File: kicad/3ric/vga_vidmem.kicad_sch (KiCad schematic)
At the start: 13 parts

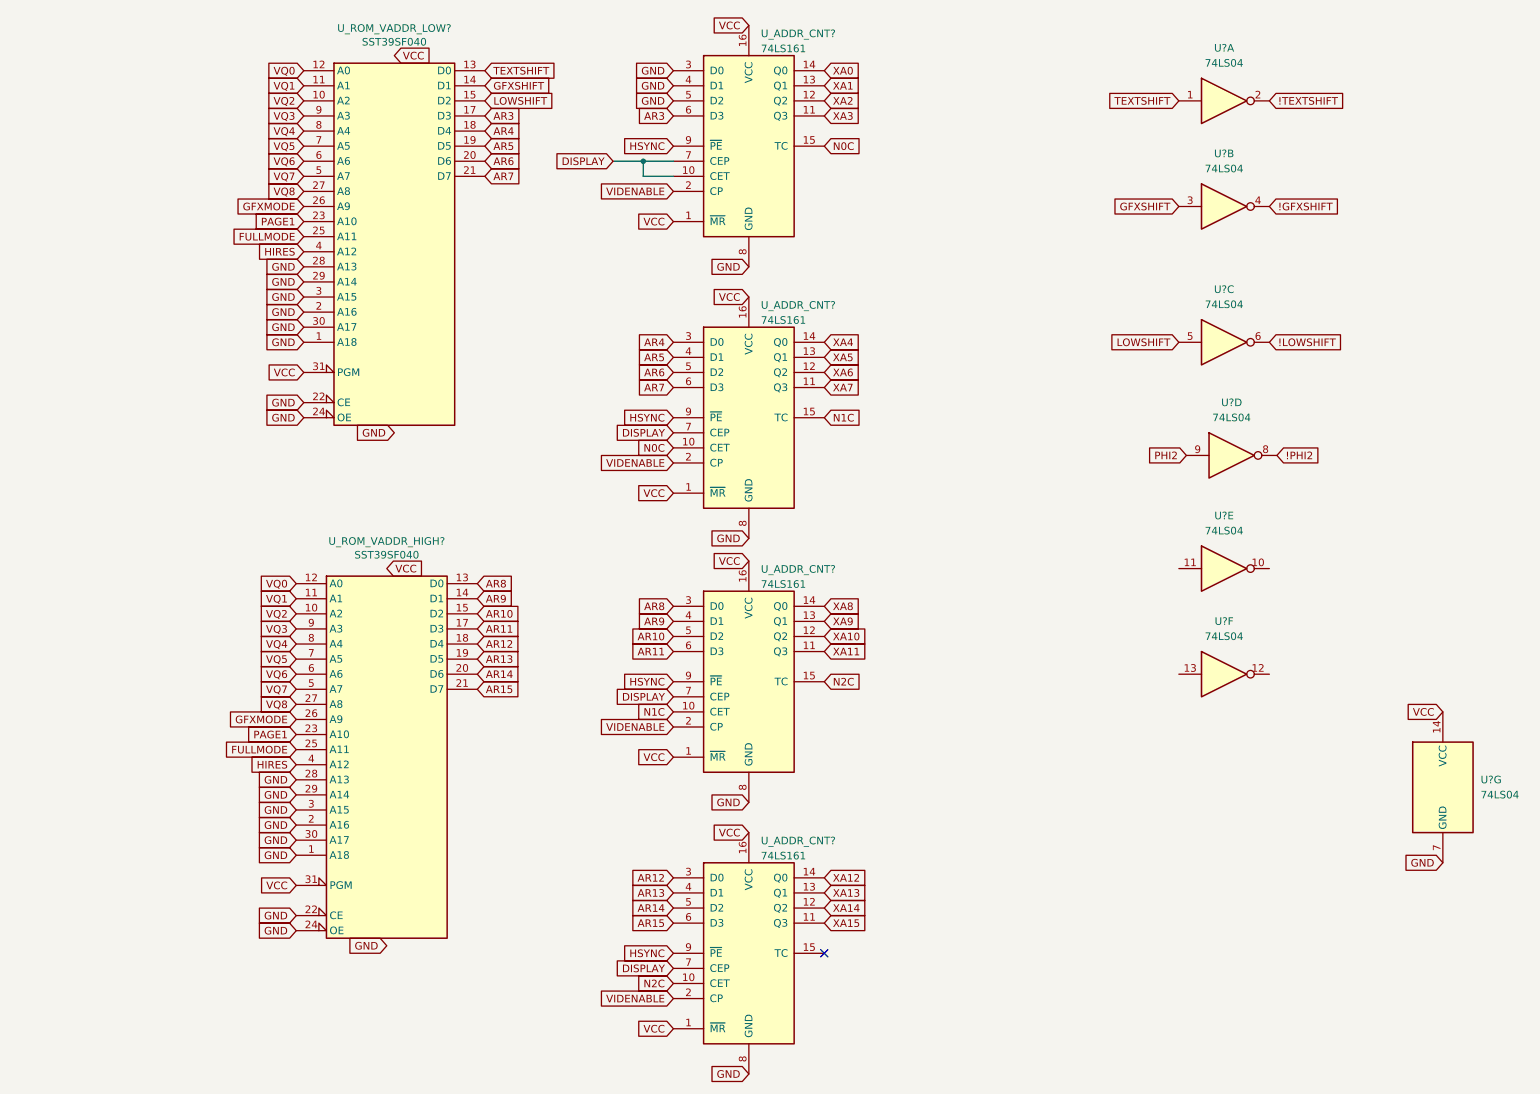
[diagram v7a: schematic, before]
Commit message: update schematic based on breadboard
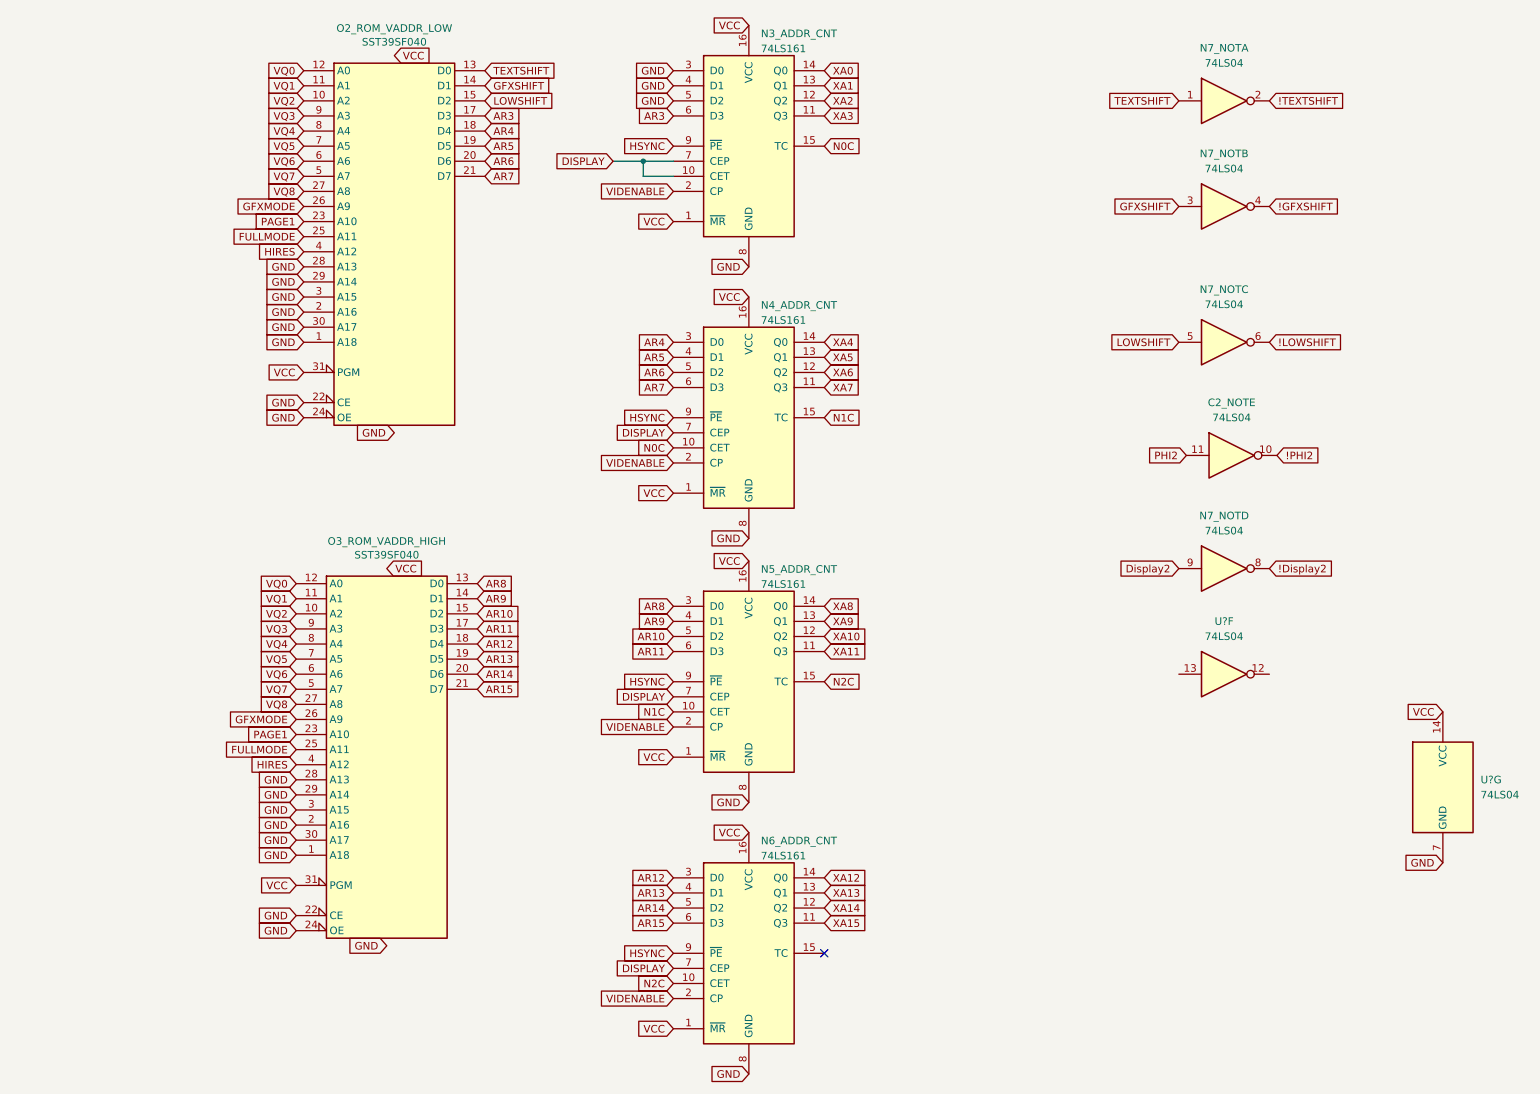
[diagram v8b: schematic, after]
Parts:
- gave numbers to parts that had none: 8
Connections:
- net !PHI2: now also C2_NOT.10; no longer C2_NOT.8
- net PHI2: now also C2_NOT.11; no longer C2_NOT.9
- new net !Display2: N7_NOT.8
- new net Display2: N7_NOT.9
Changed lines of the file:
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@@
 		)
 	)
+	(global_label "!Display2"
+		(shape input)
+		(at 233.68 109.22 0)
+		(fields_autoplaced yes)
+		(effects
+			(font
+				(size 1.27 1.27)
+			)
+			(justify left)
+		)
+		(property "Intersheetrefs" "${INTERSHEET_REFS}"
+			(at 245.3132 109.22 0)
+			(effects
+				(font
+					(size 1.27 1.27)
+				)
+				(justify left)
+				(hide yes)
+			)
+		)
+	)
 	(global_label "VQ2"
 		(shape input)
@@
 		)
 	)
+	(global_label "Display2"
+		(shape input)
+		(at 218.44 109.22 180)
+		(fields_autoplaced yes)
+		(effects
+			(font
+				(size 1.27 1.27)
+			)
+			(justify right)
+		)
+		(property "Intersheetrefs" "${INTERSHEET_REFS}"
+			(at 207.4116 109.22 0)
+			(effects
+				(font
+					(size 1.27 1.27)
+				)
+				(justify right)
+				(hide yes)
+			)
+		)
+	)
 	(global_label "VQ2"
 		(shape input)
@@
 		(on_board yes)
 		(dnp no)
-		(property "Reference" "U_ROM_VADDR_LOW?"
+		(property "Reference" "O2_ROM_VADDR_LOW"
 			(at 86.36 18.2626 0)
 			(effects
@@
 			(project "3ric"
 				(path "/e63e39d7-6ac0-4ffd-8aa3-1841a4541b55/3a5ec449-df9a-4784-a739-e66dc5cc26a2"
-					(reference "U_ROM_VADDR_LOW?")
+					(reference "O2_ROM_VADDR_LOW")
 					(unit 1)
 				)
@@
 		(dnp no)
 		(fields_autoplaced yes)
-		(property "Reference" "U?"
+		(property "Reference" "N7_NOT"
 			(at 226.06 39.37 0)
 			(effects
@@
 			(project "3ric"
 				(path "/e63e39d7-6ac0-4ffd-8aa3-1841a4541b55/3a5ec449-df9a-4784-a739-e66dc5cc26a2"
-					(reference "U?")
+					(reference "N7_NOT")
 					(unit 2)
 				)
@@
 		(dnp no)
 		(fields_autoplaced yes)
-		(property "Reference" "U?"
+		(property "Reference" "N7_NOT"
 			(at 226.06 62.23 0)
 			(effects
@@
 			(project "3ric"
 				(path "/e63e39d7-6ac0-4ffd-8aa3-1841a4541b55/3a5ec449-df9a-4784-a739-e66dc5cc26a2"
-					(reference "U?")
+					(reference "N7_NOT")
 					(unit 3)
 				)
@@
 		(on_board yes)
 		(dnp no)
-		(property "Reference" "U_ROM_VADDR_HIGH?"
+		(property "Reference" "O3_ROM_VADDR_HIGH"
 			(at 85.09 104.6226 0)
 			(effects
@@
 			(project "3ric"
 				(path "/e63e39d7-6ac0-4ffd-8aa3-1841a4541b55/3a5ec449-df9a-4784-a739-e66dc5cc26a2"
-					(reference "U_ROM_VADDR_HIGH?")
+					(reference "O3_ROM_VADDR_HIGH")
 					(unit 1)
 				)
@@
 		(lib_id "74xx:74LS04")
 		(at 226.06 109.22 0)
-		(unit 5)
+		(unit 4)
 		(exclude_from_sim no)
 		(in_bom yes)
@@
 		(dnp no)
 		(fields_autoplaced yes)
-		(property "Reference" "U?"
+		(property "Reference" "N7_NOT"
 			(at 226.06 100.33 0)
 			(effects
@@
 			(project "3ric"
 				(path "/e63e39d7-6ac0-4ffd-8aa3-1841a4541b55/3a5ec449-df9a-4784-a739-e66dc5cc26a2"
-					(reference "U?")
-					(unit 5)
+					(reference "N7_NOT")
+					(unit 4)
 				)
 			)
@@
 		(dnp no)
 		(fields_autoplaced yes)
-		(property "Reference" "U_ADDR_CNT?"
+		(property "Reference" "N6_ADDR_CNT"
 			(at 148.0694 155.0502 0)
 			(effects
@@
 			(project "3ric"
 				(path "/e63e39d7-6ac0-4ffd-8aa3-1841a4541b55/3a5ec449-df9a-4784-a739-e66dc5cc26a2"
-					(reference "U_ADDR_CNT?")
+					(reference "N6_ADDR_CNT")
 					(unit 1)
 				)
@@
 		(dnp no)
 		(fields_autoplaced yes)
-		(property "Reference" "U_ADDR_CNT?"
+		(property "Reference" "N3_ADDR_CNT"
 			(at 148.0694 19.1602 0)
 			(effects
@@
 			(project "3ric"
 				(path "/e63e39d7-6ac0-4ffd-8aa3-1841a4541b55/3a5ec449-df9a-4784-a739-e66dc5cc26a2"
-					(reference "U_ADDR_CNT?")
+					(reference "N3_ADDR_CNT")
 					(unit 1)
 				)
@@
 		(dnp no)
 		(fields_autoplaced yes)
-		(property "Reference" "U?"
+		(property "Reference" "N7_NOT"
 			(at 226.06 21.59 0)
 			(effects
@@
 			(project "3ric"
 				(path "/e63e39d7-6ac0-4ffd-8aa3-1841a4541b55/3a5ec449-df9a-4784-a739-e66dc5cc26a2"
-					(reference "U?")
+					(reference "N7_NOT")
 					(unit 1)
 				)
@@
 		(dnp no)
 		(fields_autoplaced yes)
-		(property "Reference" "U_ADDR_CNT?"
+		(property "Reference" "N4_ADDR_CNT"
 			(at 148.0694 64.8802 0)
 			(effects
@@
 			(project "3ric"
 				(path "/e63e39d7-6ac0-4ffd-8aa3-1841a4541b55/3a5ec449-df9a-4784-a739-e66dc5cc26a2"
-					(reference "U_ADDR_CNT?")
+					(reference "N4_ADDR_CNT")
 					(unit 1)
 				)
@@
 		(lib_id "74xx:74LS04")
 		(at 227.33 90.17 0)
-		(unit 4)
+		(unit 5)
 		(exclude_from_sim no)
 		(in_bom yes)
@@
 		(dnp no)
 		(fields_autoplaced yes)
-		(property "Reference" "U?"
+		(property "Reference" "C2_NOT"
 			(at 227.33 81.28 0)
 			(effects
@@
 			(project "3ric"
 				(path "/e63e39d7-6ac0-4ffd-8aa3-1841a4541b55/3a5ec449-df9a-4784-a739-e66dc5cc26a2"
-					(reference "U?")
-					(unit 4)
+					(reference "C2_NOT")
+					(unit 5)
 				)
 			)
@@
 		(dnp no)
 		(fields_autoplaced yes)
-		(property "Reference" "U_ADDR_CNT?"
+		(property "Reference" "N5_ADDR_CNT"
 			(at 148.0694 109.3302 0)
 			(effects
@@
 			(project "3ric"
 				(path "/e63e39d7-6ac0-4ffd-8aa3-1841a4541b55/3a5ec449-df9a-4784-a739-e66dc5cc26a2"
-					(reference "U_ADDR_CNT?")
+					(reference "N5_ADDR_CNT")
 					(unit 1)
 				)
